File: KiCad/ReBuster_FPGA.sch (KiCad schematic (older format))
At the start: 26 parts, among them U1 10M02SCU169, U2 LM1117-3.3

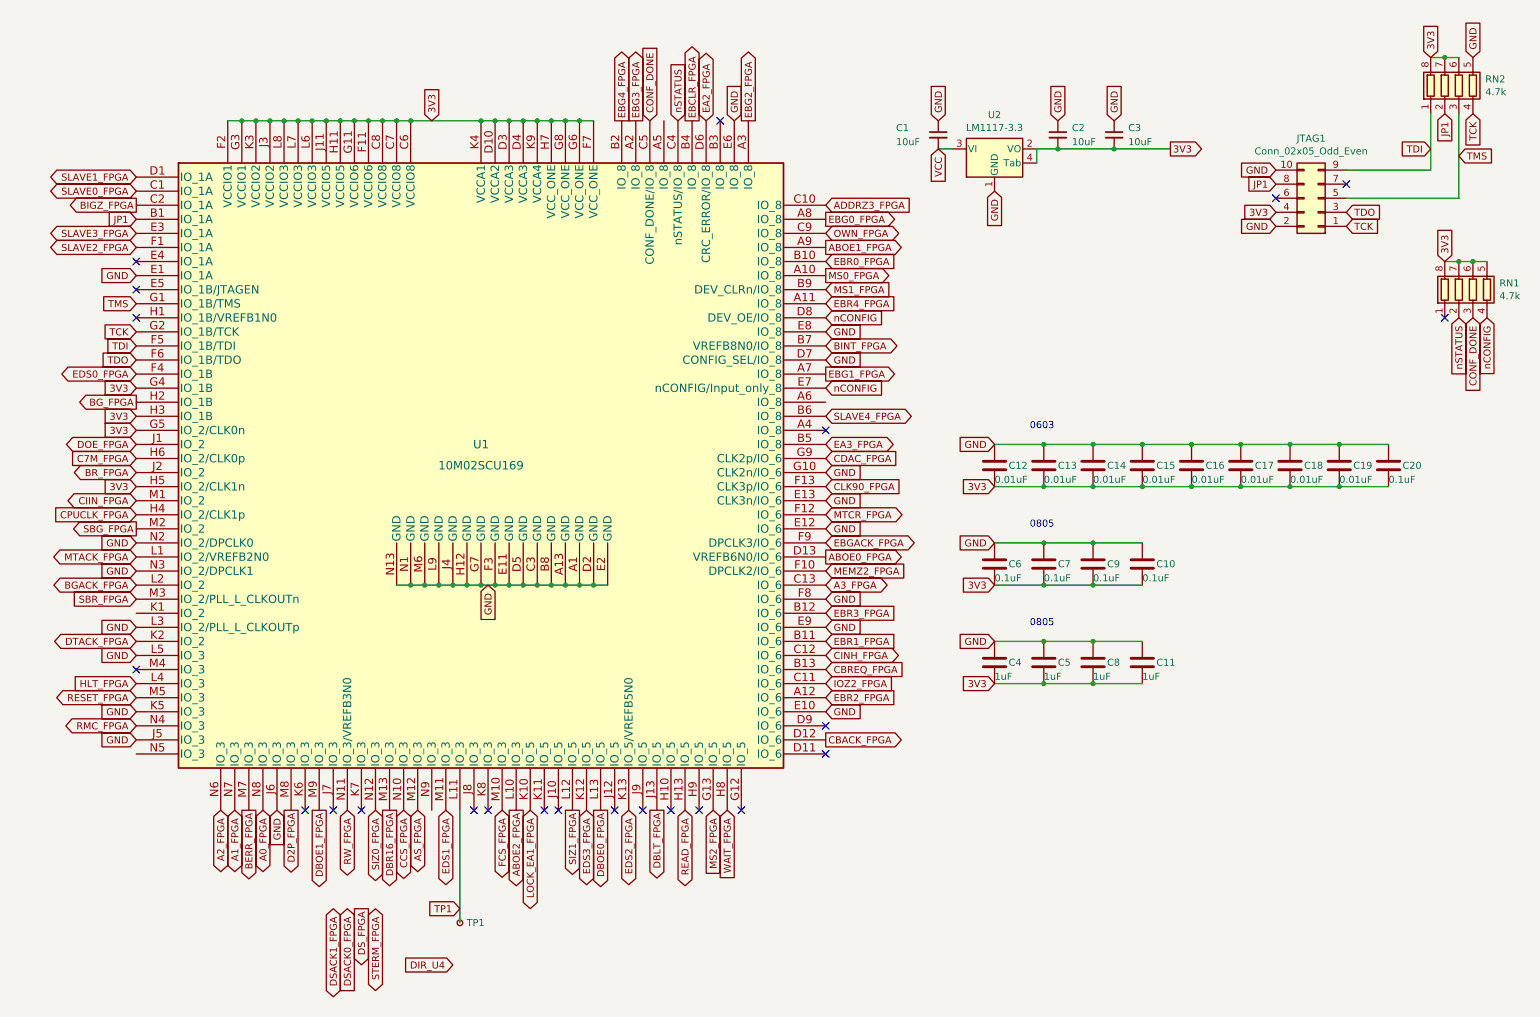
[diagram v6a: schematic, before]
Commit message: Relocate A0,A1,A2 to FPGA pin A4,A5,A6 and route traces
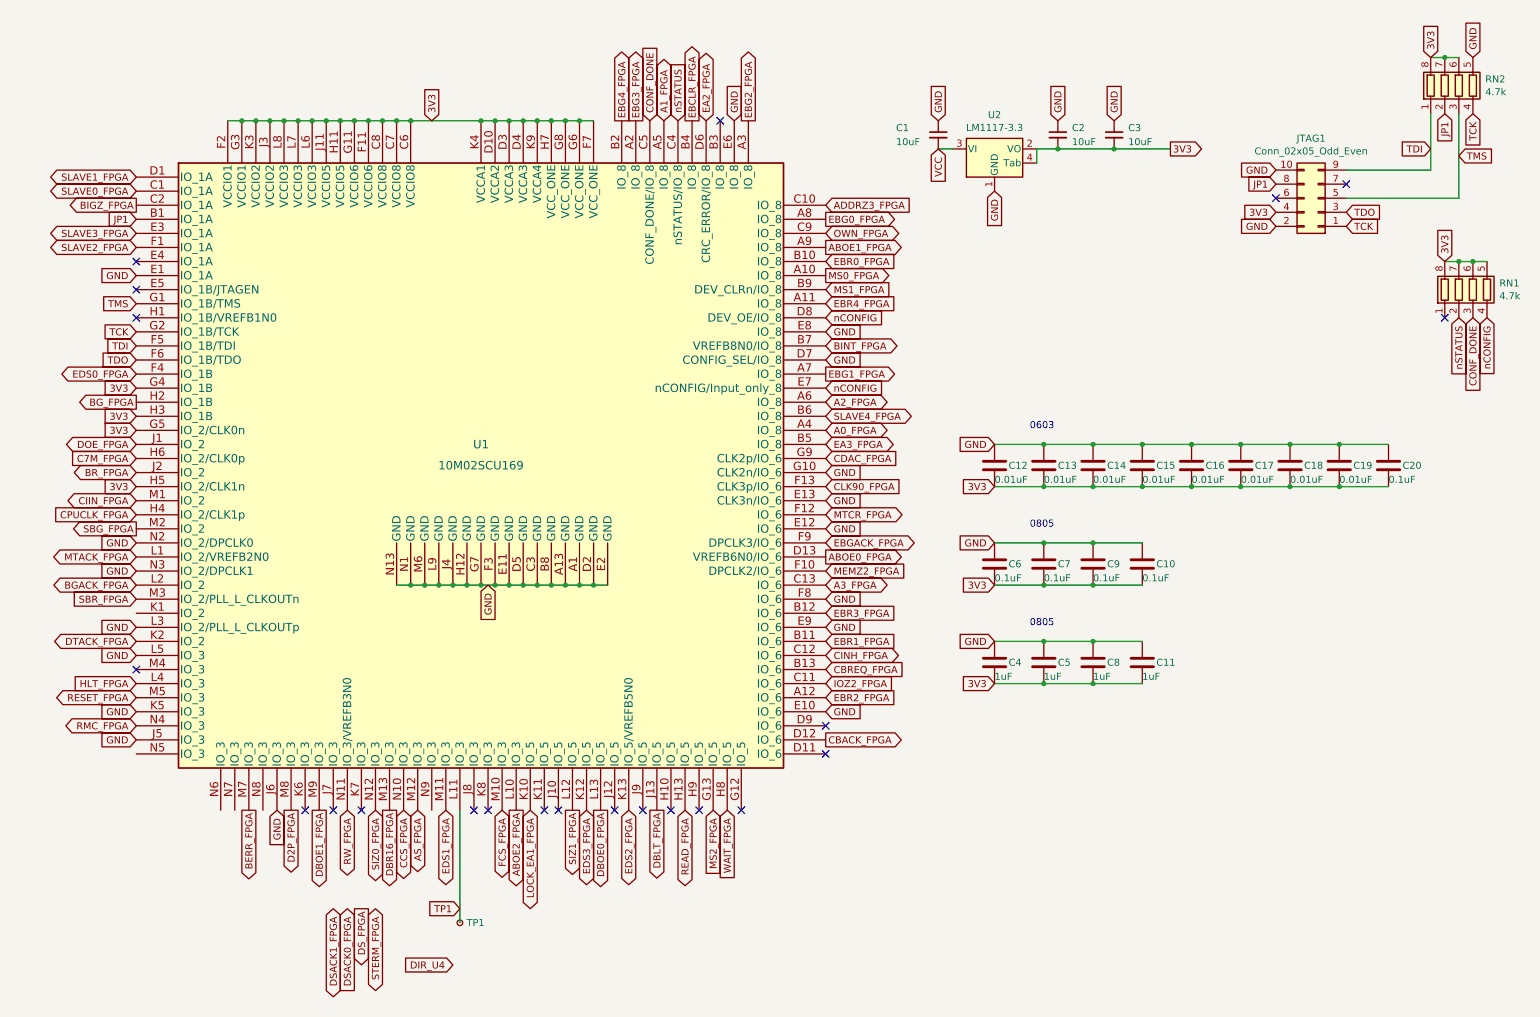
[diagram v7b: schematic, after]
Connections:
- net A0_FPGA: now also U1.A4 (IO_8); no longer U1.N8 (IO_3)
- net A1_FPGA: now also U1.A5 (IO_8); no longer U1.N7 (IO_3)
- net A2_FPGA: now also U1.A6 (IO_8); no longer U1.N6 (IO_3)
- no-connect marks 23 -> 22
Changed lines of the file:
@@
 Text GLabel 3050 6200 3    50   BiDi ~ 0
 CCS_FPGA
-Text GLabel 1750 6200 3    50   BiDi ~ 0
+Text GLabel 6050 3300 2    50   BiDi ~ 0
 A2_FPGA
-Text GLabel 1850 6200 3    50   BiDi ~ 0
+Text GLabel 4900 1300 1    50   BiDi ~ 0
 A1_FPGA
 Text GLabel 1150 4200 0    50   Output ~ 0
@@
 NoConn ~ 1150 2300
 NoConn ~ 1150 2500
-Text GLabel 2050 6200 3    50   BiDi ~ 0
+Text GLabel 6050 3500 2    50   BiDi ~ 0
 A0_FPGA
 Text GLabel 6050 2900 2    50   BiDi ~ 0
@@
 NoConn ~ 1150 5200
 NoConn ~ 3650 6200
-NoConn ~ 6050 3500
 $Comp
 L ReBuster:10M02SCU169 U1

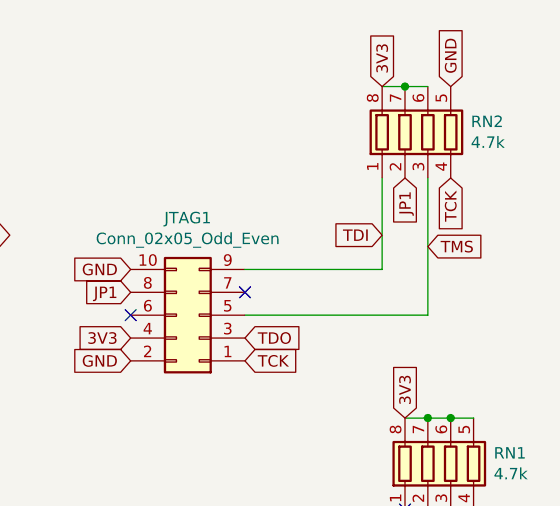
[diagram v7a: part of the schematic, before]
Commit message: Remove JP1 and assign its pull-up resistor to OE_U4
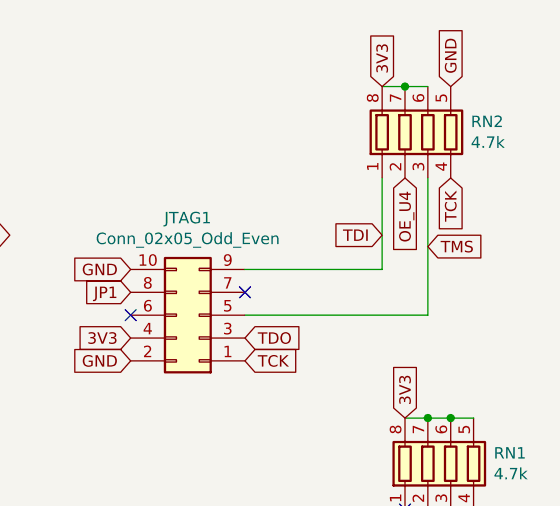
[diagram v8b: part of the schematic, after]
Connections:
- net JP1: no longer RN2.2 (R2.1)
- new net OE_U4: RN2.2 (R2.1)
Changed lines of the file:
@@
 Text GLabel 9250 1750 0    50   Input ~ 0
-JP1
-Text GLabel 10450 1250 3    50   Input ~ 0
 JP1
 Wire Wire Line
@@
 Text GLabel 3450 6900 0    50   Input ~ 0
 TP1
+Text GLabel 10450 1250 3    50   Input ~ 0
+OE_U4
 $EndSCHEMATC
